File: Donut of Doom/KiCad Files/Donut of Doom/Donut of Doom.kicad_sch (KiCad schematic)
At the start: 18 parts

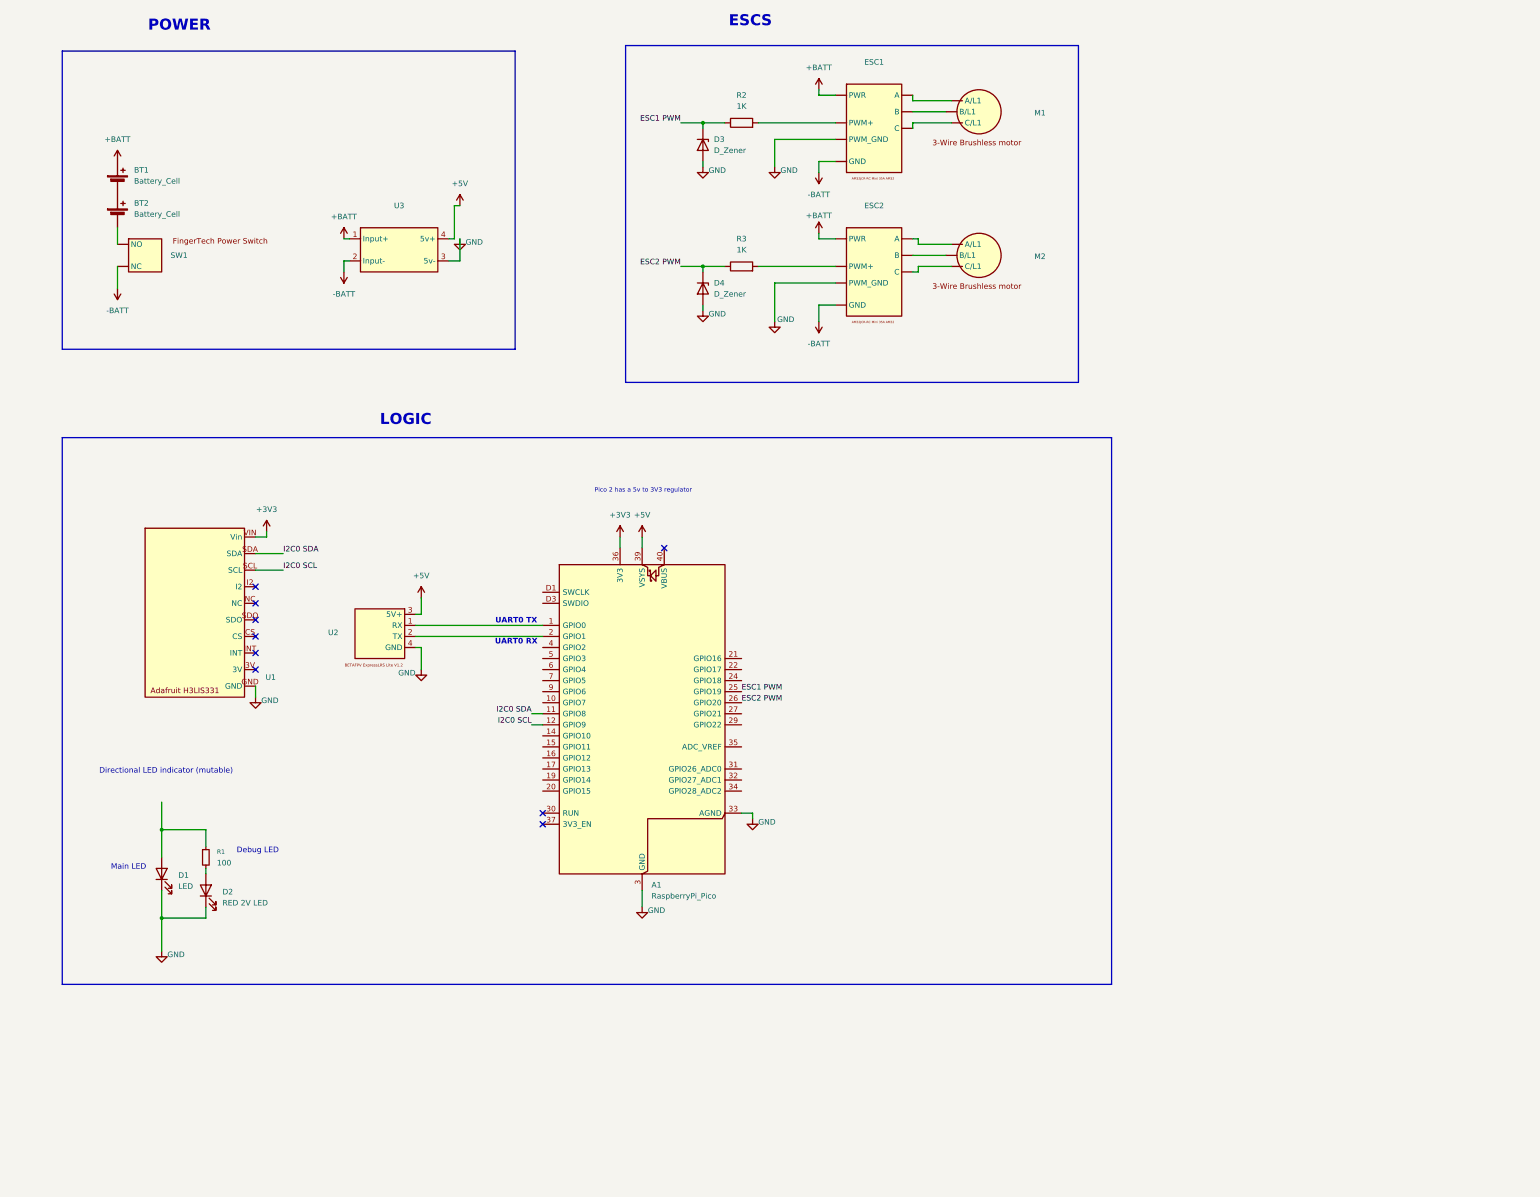
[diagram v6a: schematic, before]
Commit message: New footprints for buck and accel, layout partially done.
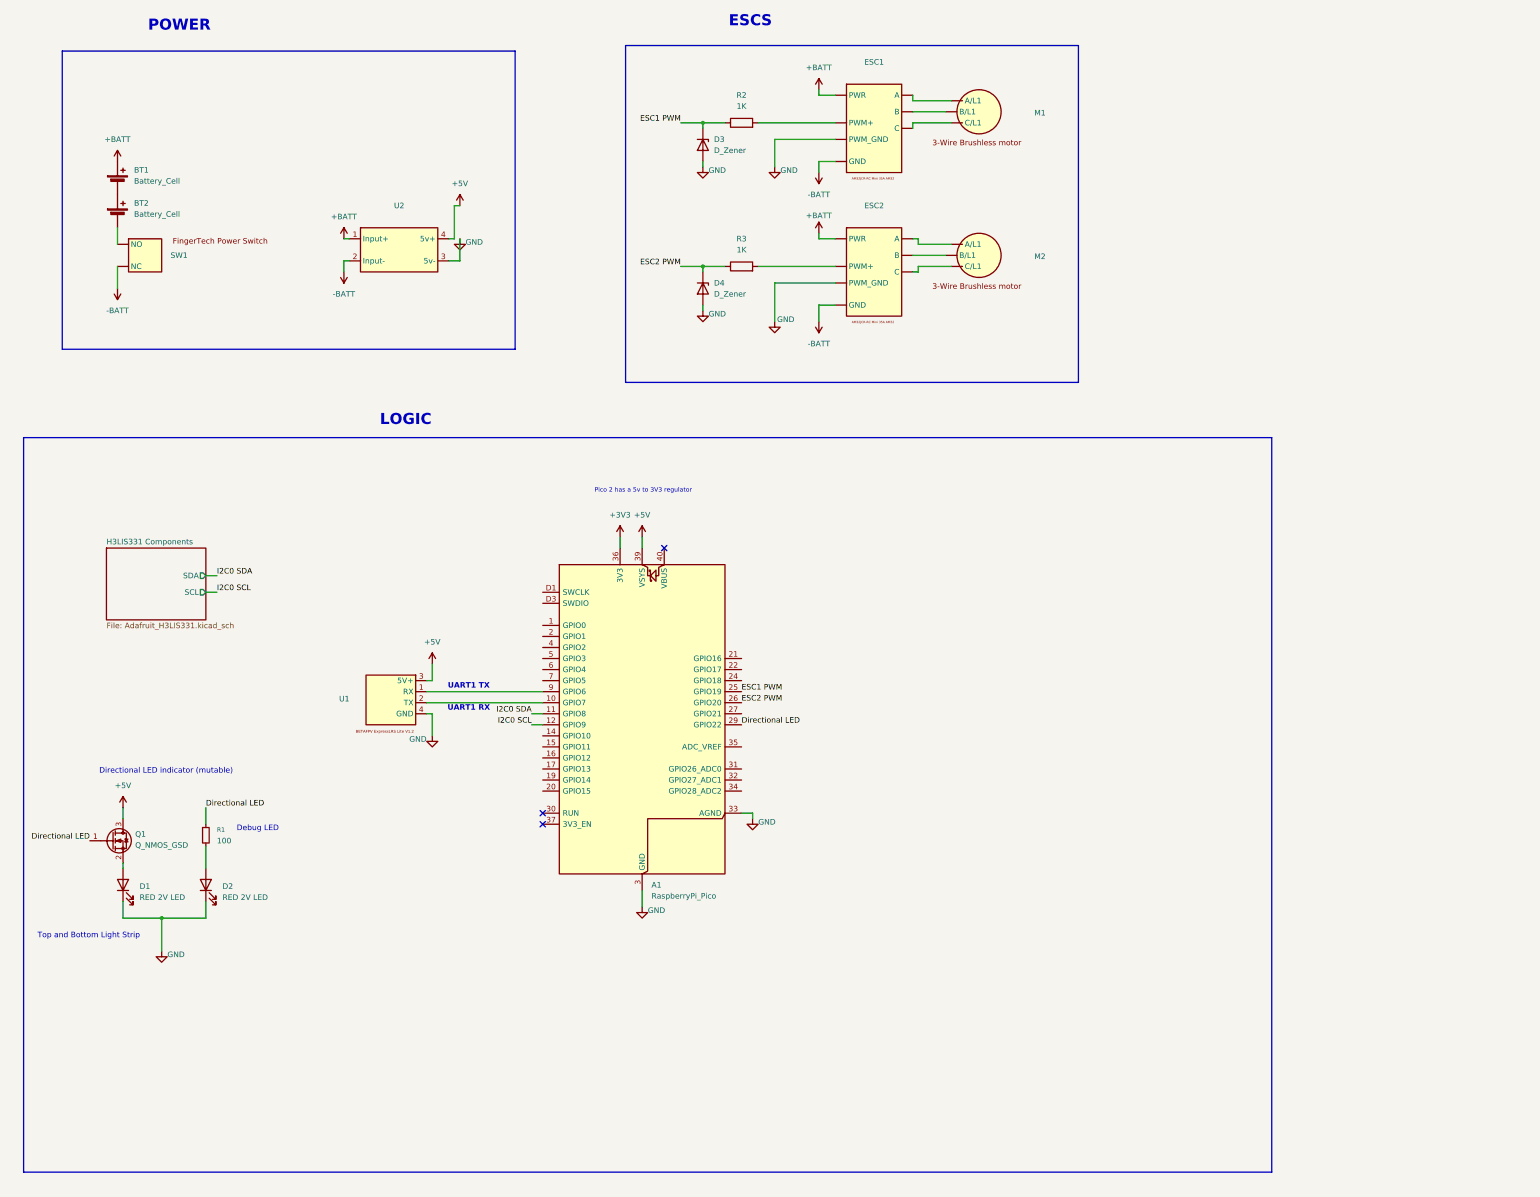
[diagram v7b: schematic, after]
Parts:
- removed U1: ~, adafruit_h3lis331:Adafruit_H3LIS331, symbol adafruit_h3lis331:Adafruit_H3LIS331
- added Q1: Q_NMOS_GSD, Package_TO_SOT_SMD:SOT-23_Handsoldering, symbol Transistor_FET:Q_NMOS_GSD
- D1: value LED -> RED 2V LED; footprint (none) -> Battlebots:2 pth Pads
- renumbered U2 to U1, U3 to U2
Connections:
- net +5V: now also Q1.3 (D)
- net at A1.1 (GPIO0): no longer U1.1 (RX)
- net at A1.10 (GPIO7): now also U1.2 (TX)
- net at A1.2 (GPIO1): no longer U1.2 (TX)
- net Directional LED: now reaches A1.29 (GPIO22)
- net Directional LED: now also R1.1, Q1.1 (G)
- net at A1.9 (GPIO6): now also U1.1 (RX)
- net at D1.2 (A): now also Q1.2 (S); no longer R1.1
- new net: ESC1. (C), M1. (C/L1) (x2)
- new net: ESC2. (C), M2. (C/L1) (x2)
- no-connect marks 9 -> 3
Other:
- added sheet H3LIS331 Components (Adafruit_H3LIS331.kicad_sch)
- note added: "Top and Bottom Light Strip"
- note added: "UART1 RX"
- note added: "UART1 TX"
- note removed: "Main LED"
- note removed: "UART0 RX"
- note removed: "UART0 TX"
- moved on the sheet: D2, R1, U1

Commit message: PCB almost finalized, awaiting dfm
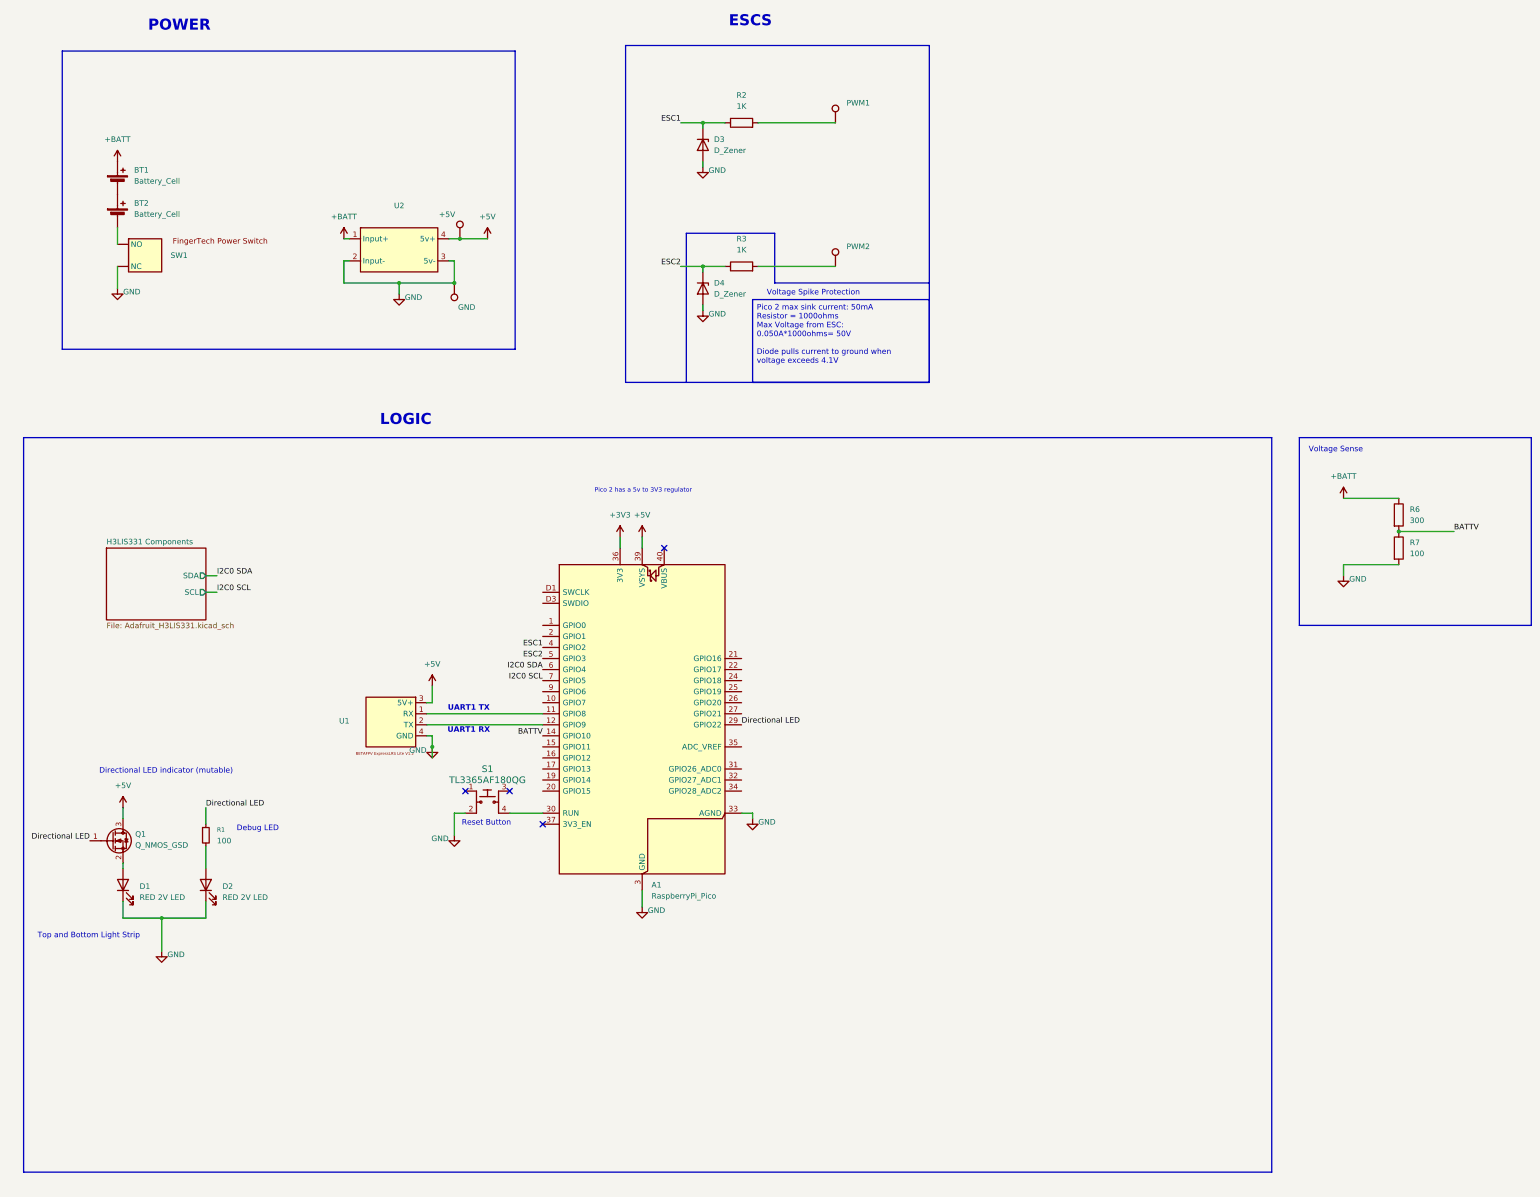
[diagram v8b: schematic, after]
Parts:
- removed ESC1, ESC2: ~, symbol Battlebots Symbols:jcr_rc_mini_35A_am32
- removed M1, M2: ~, symbol Battlebots Symbols:Generic_3_Wire_Brushless_motor
- added PWM1, PWM2: ~, Battlebots:Oval Pad, symbol Connector:TestPoint
- added R6: 300, Resistor_SMD:R_0603_1608Metric_Pad0.98x0.95mm_HandSolder, symbol Device:R
- added R7: 100, Resistor_SMD:R_0603_1608Metric_Pad0.98x0.95mm_HandSolder, symbol Device:R
- added S1: TL3365AF180QG, TL3365AF180QG:SW_TL3365AF180QG, symbol dk_Tactile-Switches:TL3315NF160Q
- added TP3: +5V, TestPoint:TestPoint_Pad_D2.0mm, symbol Connector:TestPoint
- added TP4: GND, TestPoint:TestPoint_Pad_D3.0mm, symbol Connector:TestPoint
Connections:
- net -BATT is gone; now on net GND: SW1. (NC), U2.2 (Input-)
- net +5V: now also TP3.1
- net +BATT: now also R6.1
- net GND: now also R7.2, S1.2, TP4.1
- net I2C0 SCL: now also A1.7 (GPIO5); no longer A1.12 (GPIO9)
- net I2C0 SDA: now also A1.6 (GPIO4); no longer A1.11 (GPIO8)
- net at R3.2: now also PWM2.1
- net at A1.10 (GPIO7): no longer U1.2 (TX)
- net BATTV: now reaches A1.14 (GPIO10)
- net BATTV: now also R6.2, R7.1
- net at A1.30 (RUN): now also S1.4
- net ESC1: now reaches A1.4 (GPIO2)
- net ESC1: now also D3.1 (K), R2.1
- net ESC2: now reaches A1.5 (GPIO3)
- net ESC2: now also D4.1 (K), R3.1
- net at U1.1 (RX): now also A1.11 (GPIO8); no longer A1.9 (GPIO6)
- net at R2.2: now also PWM1.1
- removed net ESC1 PWM: A1.25 (GPIO19), D3.1 (K), R2.1
- removed net ESC2 PWM: A1.26 (GPIO20), D4.1 (K), R3.1
- new net: A1.12 (GPIO9), U1.2 (TX)
- no-connect marks 3 -> 4
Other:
- note added: "Reset Button"
- note added: "Voltage Sense"
- note added: "Voltage Spike Protection"
- moved on the sheet: U1
